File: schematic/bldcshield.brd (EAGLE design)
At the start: 90.2 x 53.3 mm, 45 parts, among them IC1 IR2101SMD, IC2 IR2101SMD, IC3 IR2101SMD, Q3 Shield

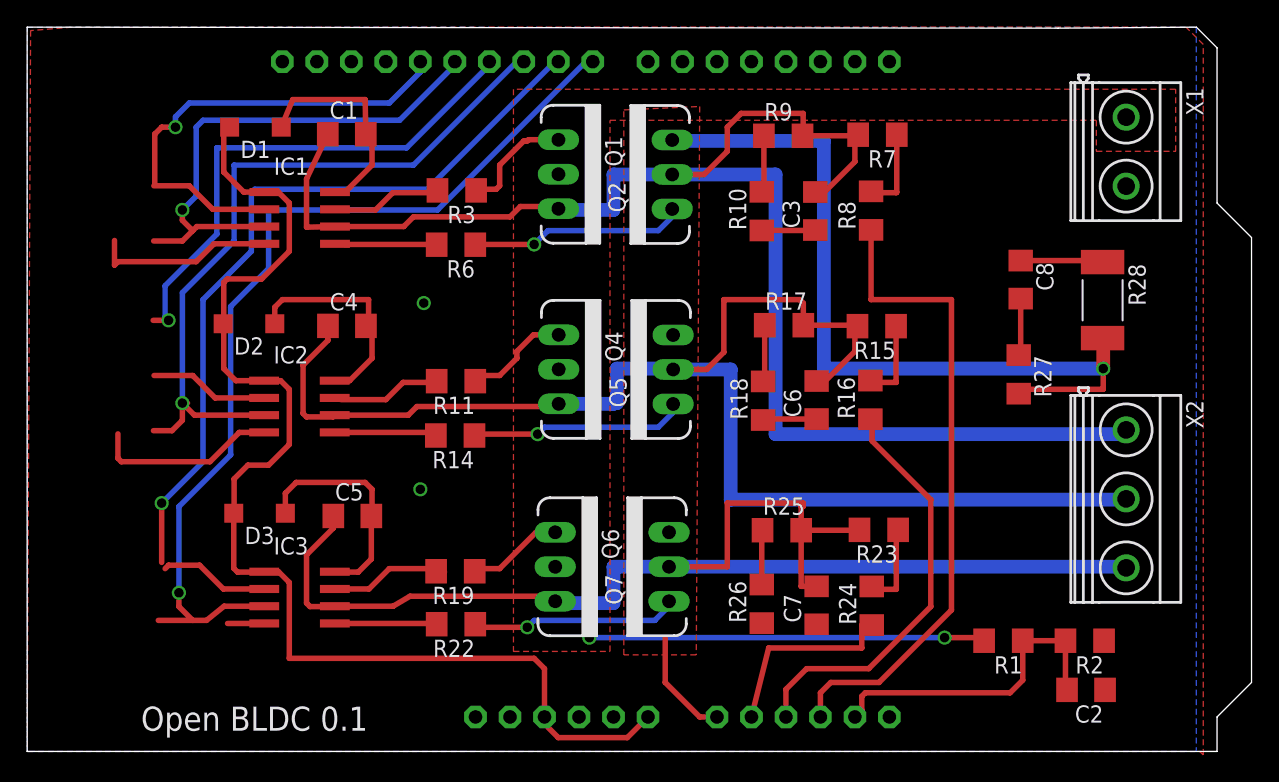
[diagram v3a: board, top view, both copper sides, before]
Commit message: updated schematic
updated schematic: removed pull down resistors and added 12V regulator
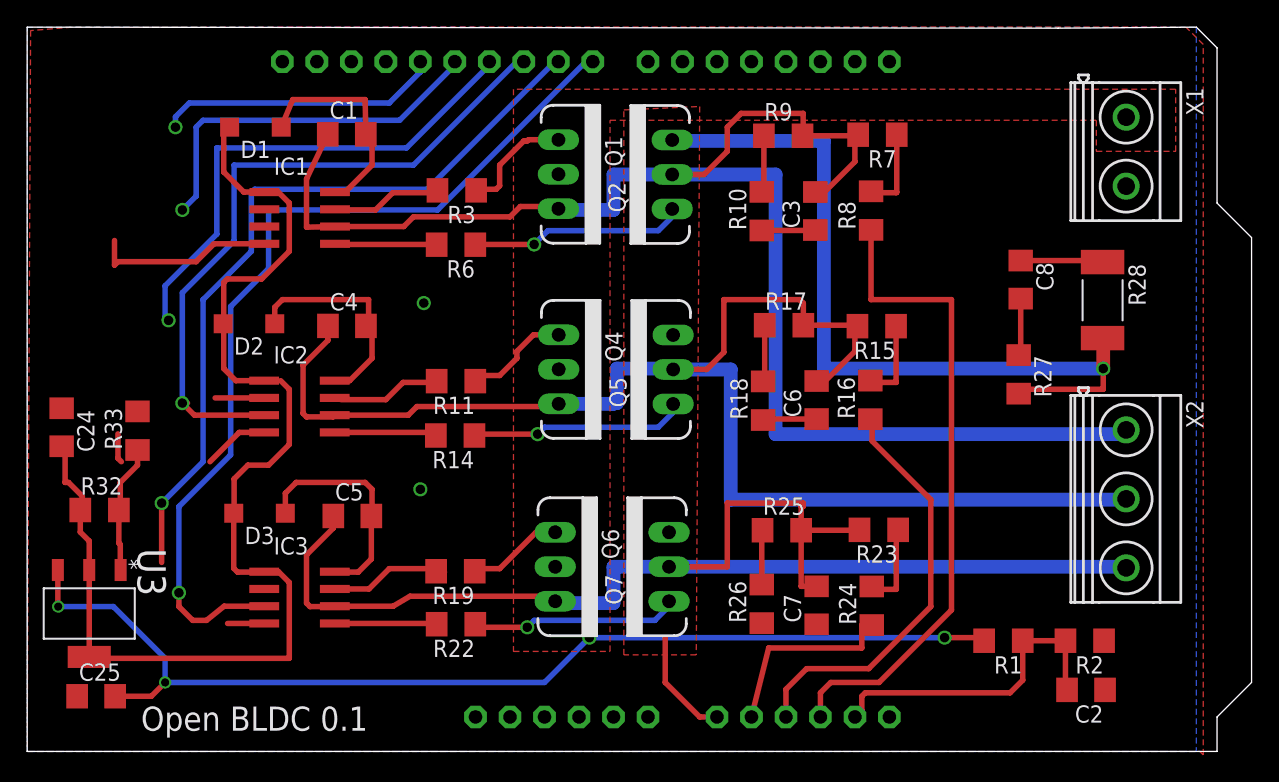
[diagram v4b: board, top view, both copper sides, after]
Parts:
- added C24: 1uF, SmartPrj:C1206
- added C25: 0.1u, SmartPrj:C1206
- added R32: 240, SmartPrj:R1206
- added R33: 2.2k, SmartPrj:R1206
- added U3: LM317DCY, Texas Instruments_By_element14_Batch_1:SOT230P700X180-4N
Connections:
- new net +12V: C24.2, D1.A, D2.A, D3.A, IC1.1, IC2.1, IC3.1, R32.1, U3.2, U3.4
- new net N$5: R32.2, R33.1, U3.1
- net +5V: no longer D1.A, D2.A, D3.A, IC1.1, IC2.1, IC3.1
- net GND: now also C24.1, C25.1, R33.2
- net VCC: now also C25.2, U3.3
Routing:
- net +5V: track 88.2 -> 0.00 mm
- net +12V: track 0.00 -> 85.6 mm
- net VCC: track 29.3 -> 79.9 mm, vias 2 -> 4
- net HI_1: track 35.2 -> 20.9 mm
- net LO_1: track 38.1 -> 27.7 mm
- net N$5: track 0.00 -> 9.46 mm
- net HI_3: track 64.7 -> 56.6 mm
- net GND: track 45.0 -> 38.5 mm
- net HI_2: track 47.2 -> 40.8 mm
- net LO_2: track 54.1 -> 50.4 mm
- net LO_3: track 70.0 -> 67.4 mm

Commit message: updated schematic and code
added hall effect sensors
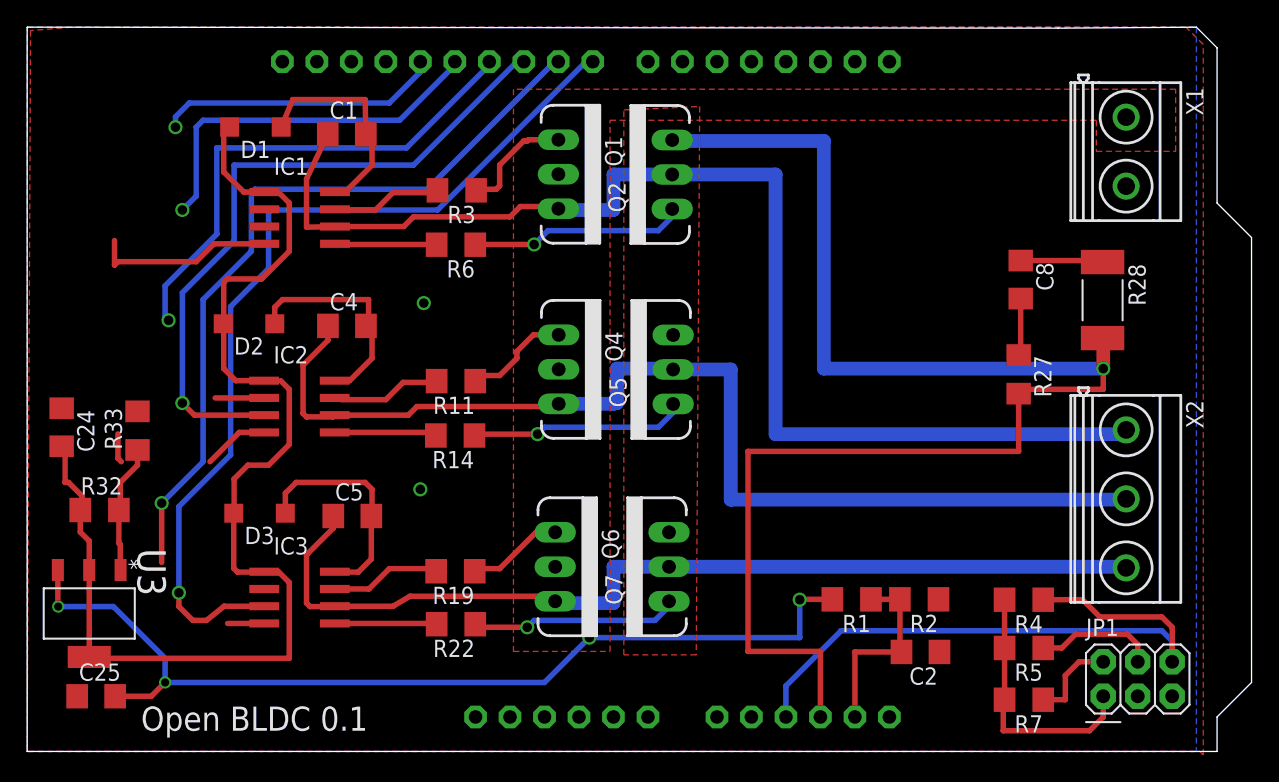
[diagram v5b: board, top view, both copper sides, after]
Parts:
- removed C3, C6, C7: 100pF, SmartPrj:C1206
- removed R10, R17, R18, R25, R26, R9: 22k, SmartPrj:R1206
- removed R15, R23: 100k, SmartPrj:R1206
- removed R16, R24, R8: 15k, SmartPrj:R1206
- added JP1: (no value), SparkFun-Connectors:2X03
- added R4, R5: 10k, SmartPrj:R1206
- R7: value 100k -> 10k
- moved R7 43.0 mm to (101.3, 30.5)
- moved R2 12.6 mm to (93.6, 37.9)
- moved C2 12.5 mm to (93.7, 34.0)
- moved R1 11.6 mm to (88.7, 37.9)
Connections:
- removed net EMF1: Q3.A3, R8.1
- removed net EMF2: Q3.A2, R16.1
- removed net EMF3: Q3.A1, R24.1
- removed net N$12: R17.1, R18.2
- removed net N$19: R15.1, R16.2
- removed net N$2: R10.2, R9.1
- removed net N$26: R25.1, R26.2
- removed net N$28: R23.1, R24.2
- new net N$4: JP1.2, Q3.A0, R7.1
- new net N$7: JP1.6, Q3.A2, R4.1
- net +5V: now also JP1.1, R4.2, R5.2, R7.2
- net BLDC1: no longer C3.2, R7.2, R9.2
- net BLDC2: no longer C6.2, R15.2, R17.2
- net BLDC3: no longer C7.2, R23.2, R25.2
- net CURRENT: now also Q3.A3; no longer Q3.A0
- net GND: now also JP1.5; no longer C3.1, C6.1, C7.1, R10.1, R18.1, R26.1
- net N$10: now also JP1.4, Q3.A1, R5.1; no longer R7.1, R8.2
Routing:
- net EMF1: track 47.9 -> 0.00 mm
- net N$7: track 0.00 -> 47.1 mm
- net CURRENT: track 66.9 -> 107.8 mm
- net EMF2: track 31.4 -> 0.00 mm
- net BLDC3: track 97.3 -> 71.0 mm
- net BLDC2: track 106.0 -> 80.6 mm
- net BLDC1: track 115.3 -> 90.8 mm
- net +5V: track 0.00 -> 19.0 mm
- net EMF3: track 14.5 -> 0.00 mm
- net LOW_VOLTAGE: track 23.8 -> 14.3 mm
- net VCC: track 79.9 -> 71.4 mm
- net GND: track 38.5 -> 29.9 mm
- net N$4: track 0.00 -> 6.62 mm
- net N$28: track 6.54 -> 0.00 mm
- net N$19: track 6.11 -> 0.00 mm
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
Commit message: continuing to work on pcb
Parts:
- moved R2 0.51 mm to (94.1, 37.9)
- moved C2 0.51 mm to (94.2, 34.0)
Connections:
- net N$4: now also Q3.A2; no longer Q3.A0
- net N$7: now also Q3.A0; no longer Q3.A2
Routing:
- net +5V: track 19.0 -> 65.0 mm
- net N$10: track 8.97 -> 41.8 mm
- net N$4: track 6.62 -> 32.2 mm
- net GND: track 29.9 -> 6.45 mm, vias 2 -> 3
- net HI_1: track 20.9 -> 31.1 mm
- net HI_2: track 40.8 -> 48.1 mm
- net HI_3: track 56.6 -> 63.7 mm
- net LO_1: track 27.7 -> 34.3 mm
- net N$7: track 47.1 -> 52.8 mm
- net VCC: track 71.4 -> 74.0 mm
- net LOW_VOLTAGE: track 14.3 -> 16.0 mm
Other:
- board text added: "Open BLDC 0.2"
- board text removed: "Open BLDC 0.1"

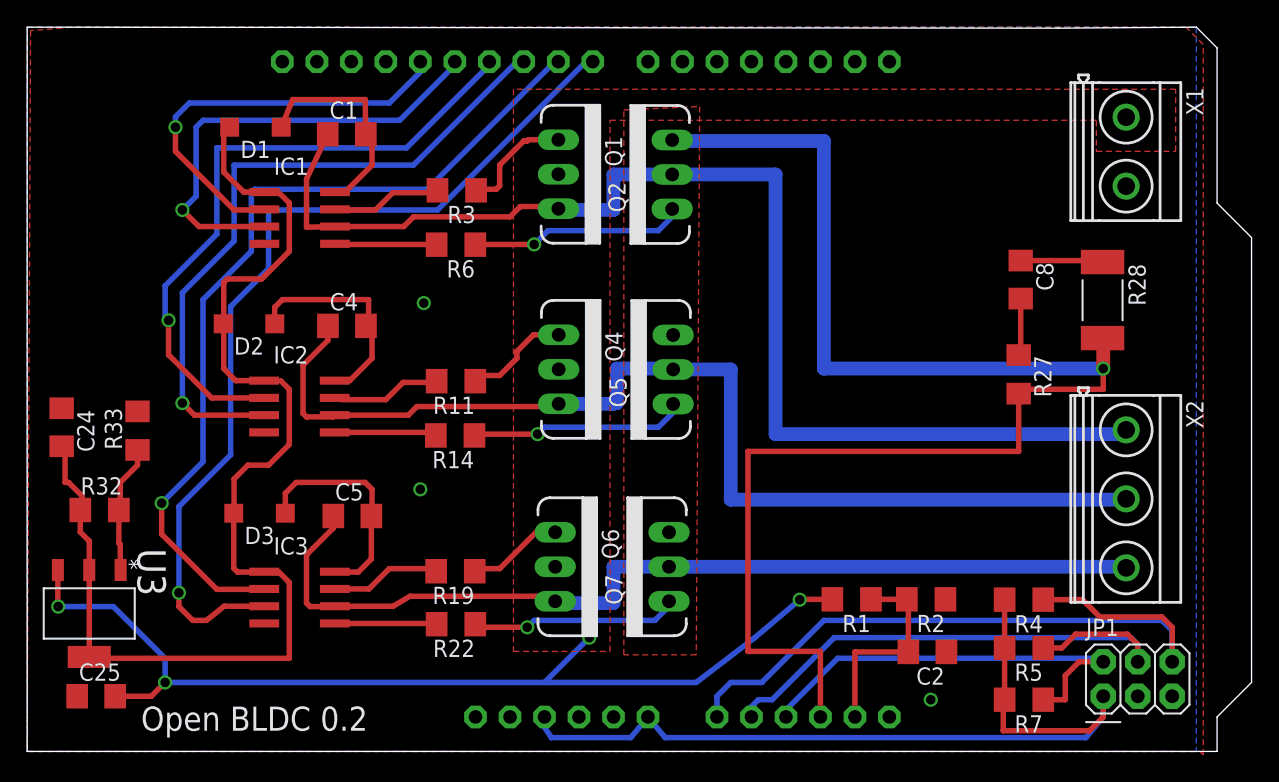
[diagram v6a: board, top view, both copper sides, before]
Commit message: changed to d-paks on both sides of the board, working on traces. moved to eagle 7.6
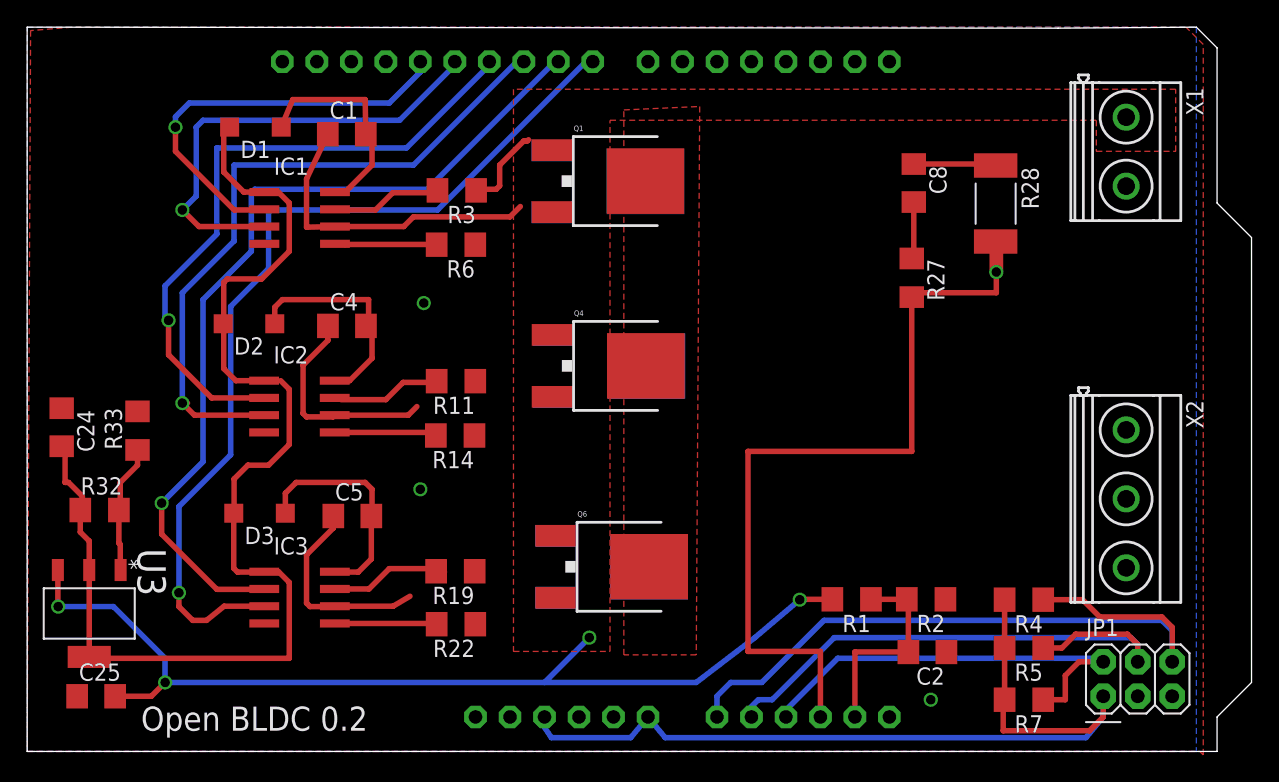
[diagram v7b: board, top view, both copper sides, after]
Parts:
- Q1, Q2, Q4, Q5, Q6, Q7: value (none) -> MOSFET-NCHANNELFDD8580; device SparkFun:TO220V -> SparkFun:DPAK
- moved R28 10.6 mm to (99.3, 67.0)
- moved R27 10.6 mm to (93.1, 61.6)
- moved C8 10.6 mm to (93.2, 68.5)
- moved Q6 5.33 mm to (72.2, 40.3)
- moved Q1 4.85 mm to (71.9, 68.7)
- moved Q4 4.83 mm to (71.9, 55.1)
- moved Q2 3.59 mm to (71.9, 68.7), flipped to the bottom
- moved Q5 3.57 mm to (72.0, 55.1), flipped to the bottom
- moved Q7 3.05 mm to (72.2, 40.3), flipped to the bottom
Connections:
- net BLDC1: now also Q2.4; no longer Q2.2
- net BLDC2: now also Q5.4; no longer Q5.2
- net BLDC3: now also Q7.4; no longer Q7.2
- net VCC: now also Q1.4, Q4.4, Q6.4; no longer Q1.2, Q4.2, Q6.2
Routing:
- net BLDC1: track 90.8 -> 23.6 mm
- net BLDC2: track 80.6 -> 16.0 mm
- net BLDC3: track 71.0 -> 15.2 mm
- net CURRENT: track 107.8 -> 58.5 mm
- net N$23: track 16.0 -> 0.00 mm, vias 1 -> 0
- net N$31: track 15.9 -> 0.00 mm, vias 1 -> 0
- net N$15: track 15.4 -> 0.00 mm, vias 1 -> 0
- net N$1: track 7.85 -> 0.59 mm
- net N$14: track 7.12 -> 0.00 mm
- net N$30: track 8.50 -> 6.30 mm

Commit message: change fets to dpaks and changed the layout with multiple pours.
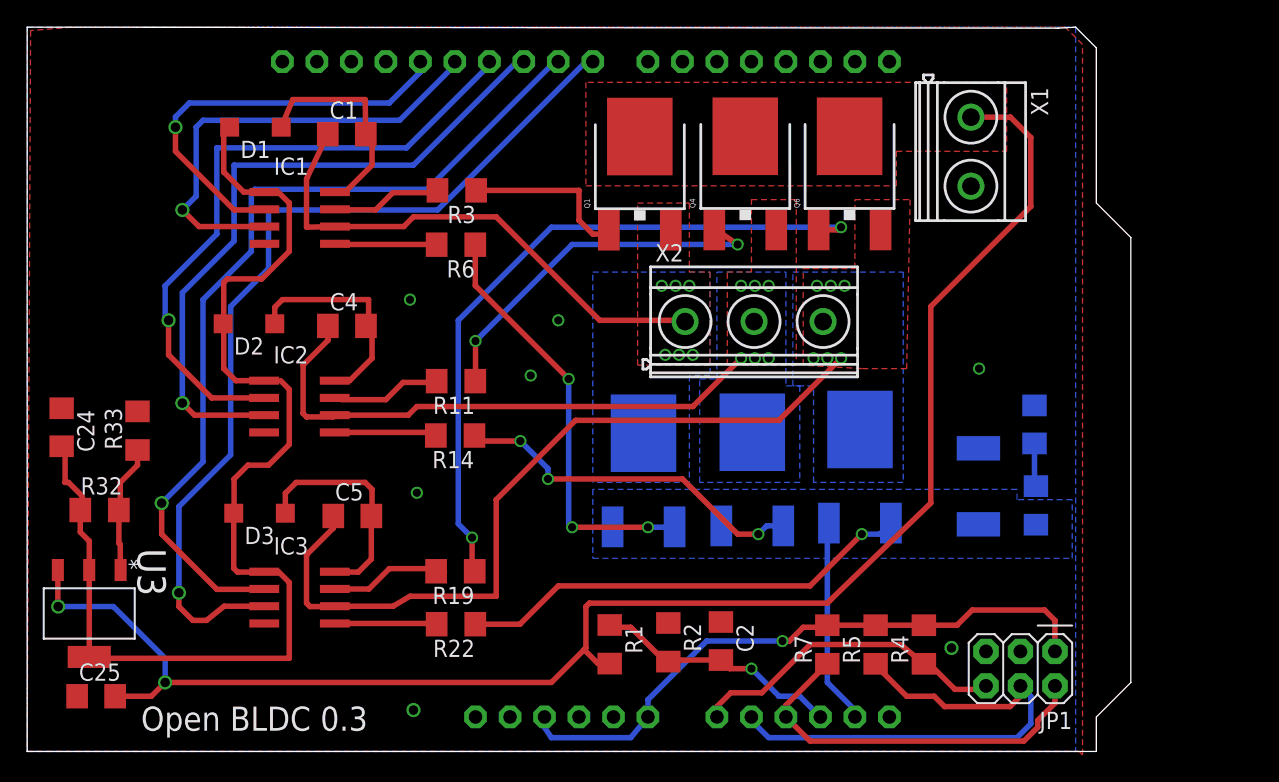
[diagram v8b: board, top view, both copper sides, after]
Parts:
- moved Q6 34.3 mm to (88.5, 70.4), turned to 0 degrees
- moved X2 29.3 mm to (84.0, 58.3), turned to 0 degrees
- moved R28 20.9 mm to (98.0, 46.2), flipped to the bottom
- moved Q2 20.2 mm to (73.3, 48.5), turned to 0 degrees
- moved C8 19.9 mm to (102.1, 50.8), flipped to the bottom
- moved R2 19.2 mm to (75.2, 34.7), turned to 270 degrees
- moved Q7 19.1 mm to (89.3, 48.8), turned to 0 degrees
- moved R27 19.1 mm to (102.2, 44.8), flipped to the bottom
- moved R1 18.1 mm to (70.8, 34.6), turned to 270 degrees
- moved Q4 17.7 mm to (80.8, 70.4), turned to 0 degrees
- moved C2 15.2 mm to (79.0, 34.8), turned to 270 degrees
- moved R7 15.0 mm to (86.9, 34.5), turned to 90 degrees
- moved X1 11.4 mm to (97.4, 70.8)
- moved Q5 11.4 mm to (81.3, 48.6), turned to 0 degrees
- moved R5 10.9 mm to (90.4, 34.5), turned to 90 degrees
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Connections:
- net CURRENT: now also Q3.A4; no longer Q3.A3
- net LOW_VOLTAGE: now also Q3.A3; no longer Q3.A4
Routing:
- net N$14: track 0.00 -> 51.8 mm, vias 0 -> 2
- net VCC: track 74.0 -> 118.9 mm, vias 4 -> 2
- net CURRENT: track 58.5 -> 15.2 mm, vias 1 -> 0
- net BLDC3: track 15.2 -> 58.3 mm, vias 0 -> 6
- net N$15: track 0.00 -> 33.7 mm, vias 0 -> 1
- net N$31: track 0.00 -> 31.3 mm, vias 0 -> 3
- net N$7: track 52.8 -> 23.9 mm
- net N$1: track 0.59 -> 27.3 mm, vias 0 -> 2
- net N$23: track 0.00 -> 26.5 mm, vias 0 -> 3
- net BLDC2: track 16.0 -> 41.4 mm, vias 0 -> 6
- net +5V: track 65.0 -> 46.1 mm, vias 0 -> 1
- net BLDC1: track 23.6 -> 38.6 mm, vias 0 -> 6
- net GND: track 6.45 -> 0.00 mm, vias 3 -> 7
- net N$30: track 6.30 -> 12.5 mm
- net N$10: track 41.8 -> 38.0 mm
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- added copper zone on layer 1, net BLDC1
- added copper zone on layer 16, net BLDC1
- added copper zone on layer 1, net BLDC2
- added copper zone on layer 16, net BLDC2
- added copper zone on layer 1, net BLDC3
- added copper zone on layer 16, net BLDC3
- added copper zone on layer 16, net CURRENT
- removed copper zone on layer 1, net CURRENT
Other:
- board size 90.2 x 53.3 mm -> 81.3 x 53.3 mm
- board text added: "Open BLDC 0.3"
- board text removed: "Open BLDC 0.2"
